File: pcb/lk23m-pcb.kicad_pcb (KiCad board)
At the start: 2 copper layers, 76.2 x 119.1 mm, 59 parts, among them J1 Conn_01x02, SW1 RotaryEncoder_Switch_MP, SW10 SW_Push, SW11 SW_Push, SW12 SW_Push, SW13 SW_Push, SW14 SW_Push, SW15 SW_Push, SW16 SW_Push, SW17 SW_Push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

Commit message: Update LKBD libraries
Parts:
- H1, H2, H3, H4: value MountingHole -> MountingHole_Pad
- SW24: footprint LKBD_Common:SW_PUSH_1P1T_6x3.5mm -> LKBD_Common:SW_Push_1P1T_6x3.5mm
- moved SW24 3.10 mm to (60.9, 50.0)

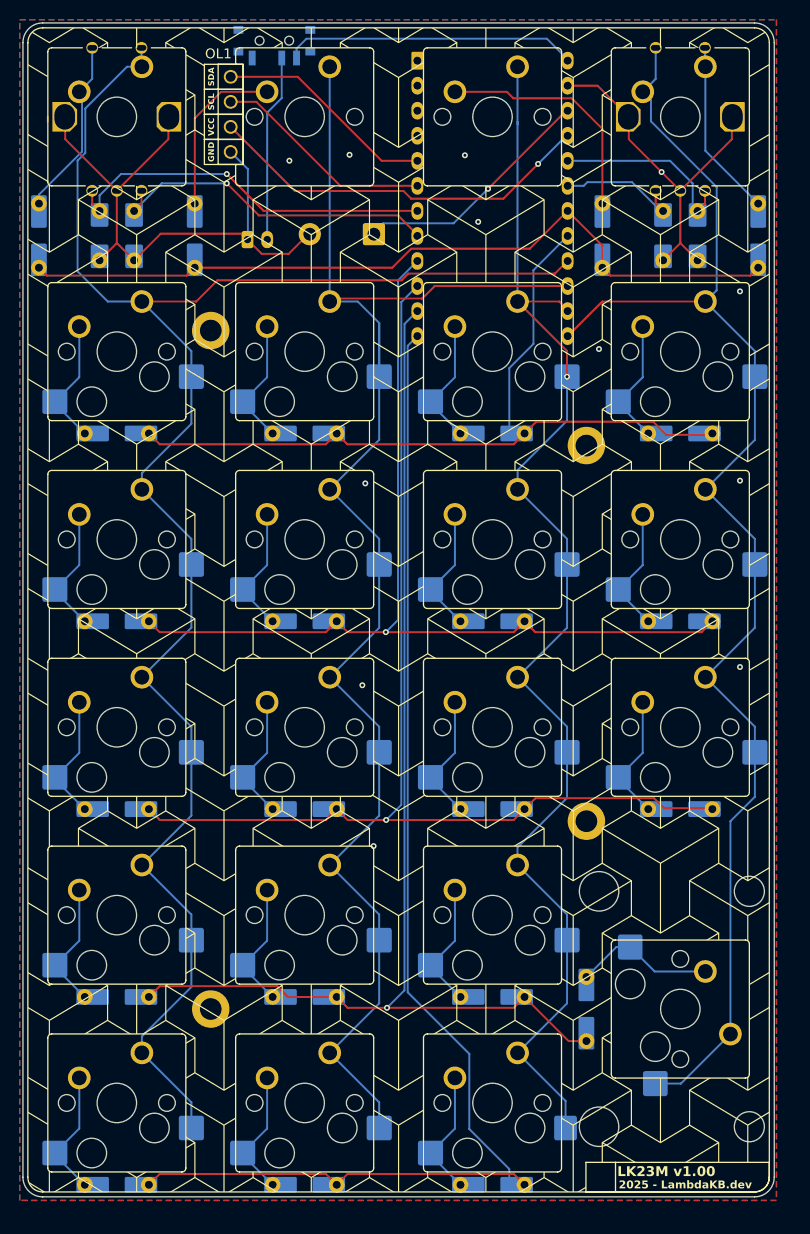
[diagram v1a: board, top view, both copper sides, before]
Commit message: Use a JST-PH Right Angle connector for battery
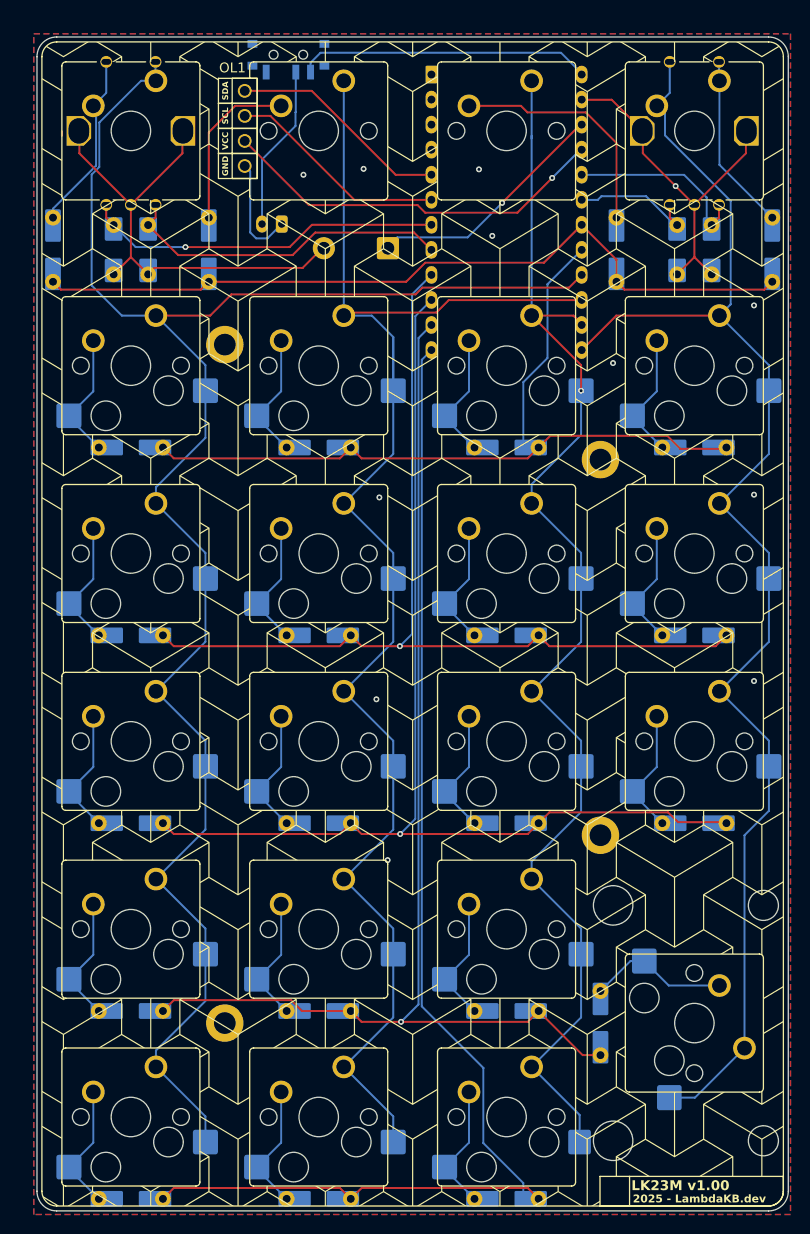
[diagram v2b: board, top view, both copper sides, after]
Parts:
- J1: footprint Connector_JST:JST_PH_B2B-PH-K_1x02_P2.00mm_Vertical -> Connector_JST:JST_PH_S2B-PH-K_1x02_P2.00mm_Horizontal
- moved J1 3.82 mm to (54.8, 49.0), turned to 180 degrees
- moved H4 2.02 mm to (87.2, 111.0)
- moved D21 2.02 mm to (58.6, 147.8)
- moved D3 2.02 mm to (88.8, 51.6)
- moved D6 2.02 mm to (58.6, 71.6)
- moved D20 2.02 mm to (39.5, 147.8)
- moved D22 2.02 mm to (77.6, 147.8)
- moved D5 2.02 mm to (39.5, 71.6)
- moved D7 2.02 mm to (77.6, 71.6)
- moved D8 2.02 mm to (96.7, 71.6)
- moved H2 2.02 mm to (87.2, 72.9)
- moved D1 2.02 mm to (31.6, 51.6)
- moved C1 2.02 mm to (37.8, 51.6)
- moved C2 2.02 mm to (41.3, 51.6)
- moved C3 2.02 mm to (94.9, 51.6)
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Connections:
- net E1S1 renamed col0
- net E2S2 renamed col3
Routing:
- net Net-(J1-Pin_2): track 19.2 -> 17.0 mm
- net E1A: track 38.6 -> 36.5 mm
- net E1B: track 34.4 -> 34.0 mm, vias 1 -> 0
